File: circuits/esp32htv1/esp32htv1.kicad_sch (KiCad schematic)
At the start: 23 parts, among them J1 Power, SW1 SW_Push, U1 BME280, U2 ESP32-WROOM-32UE, U3 LD1117S33TR_SOT223

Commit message: Second version of the ESP32 HTV project
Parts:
- removed C11, C12, C13, C14, C15: 1 uF, Capacitor_SMD:C_1206_3216Metric_Pad1.33x1.80mm_HandSolder, symbol Device:C_Polarized
- removed U4: ~, gos:DOGM132-5, symbol gos:DOGM132
- added J2: UART, Connector_PinHeader_2.54mm:PinHeader_1x04_P2.54mm_Vertical, symbol Connector:Conn_01x04_Pin
- added P1: USB_C_Plug_USB2.0, symbol Connector:USB_C_Plug_USB2.0
- added SW2: BOOT, Connector_PinSocket_2.54mm:PinSocket_1x02_P2.54mm_Vertical, symbol Switch:SW_Push
- added U4: ~, gos:DOGS102-6, symbol gos:DOGS102
- J1, SW1: footprint Connector_PinHeader_1.00mm:PinHeader_1x02_P1.00mm_Vertical -> Connector_PinSocket_2.54mm:PinSocket_1x02_P2.54mm_Vertical
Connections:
- net +3V3: now also J2.1 (Pin_1), U4.22 (VDD), U4.23 (VDD2)
- net GND: now also J2.4 (Pin_4), SW2.2, U4.20 (VSS), U4.21 (VSS); no longer C8.2, C9.2
- net at C8.1: now also U4.17 (VB0-)
- net at C10.1: now also U4.15 (VLCD)
- net at C9.1: now also U4.16 (VB1-)
- net at U2.13 (IO14): now also U4.25 (SCK)
- net at U2.23 (IO15): now also U4.28 (CS0)
- net at U2.16 (IO13): now also U4.24 (SDA)
- net at U2.25 (IO0): now also SW2.1
- net at U2.27 (IO16): now also U4.26 (CD)
- net at U2.28 (IO17): now also U4.27 (RST)
- net at U2.34 (RXD0/IO3): now also J2.3 (Pin_3)
- net at U2.35 (TXD0/IO1): now also J2.2 (Pin_2)
- new net: C8.2, U4.18 (VB0+)
- new net: P1.A1 (GND), P1.A12 (GND), P1.B1 (GND), P1.B12 (GND)
- new net: P1.A4 (VBUS), P1.A9 (VBUS), P1.B4 (VBUS), P1.B9 (VBUS)
- new net: C9.2, U4.19 (VB1+)
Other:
- note removed: "LOW POWER CONFIGURATION"
- moved on the sheet: C10, C6, C7, C8, C9, U1

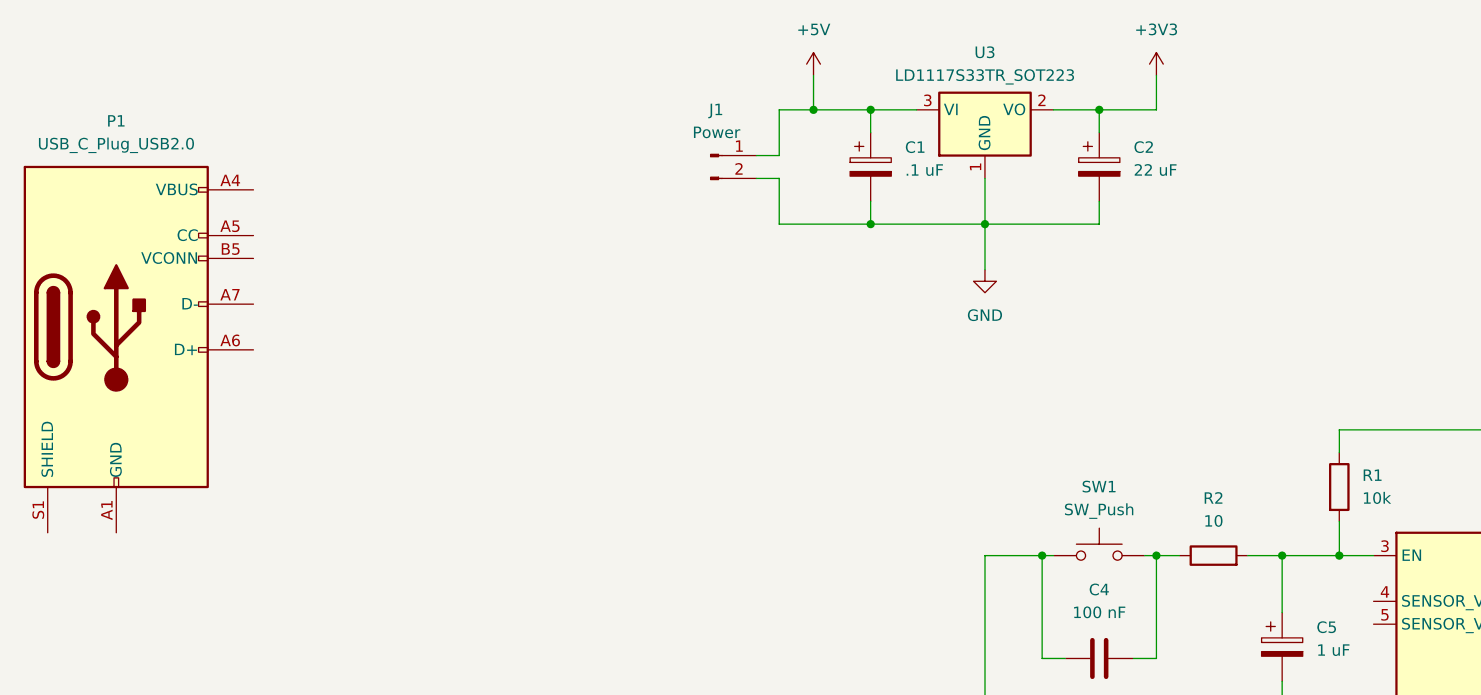
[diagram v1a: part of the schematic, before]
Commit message: Adding some sound effect circuits
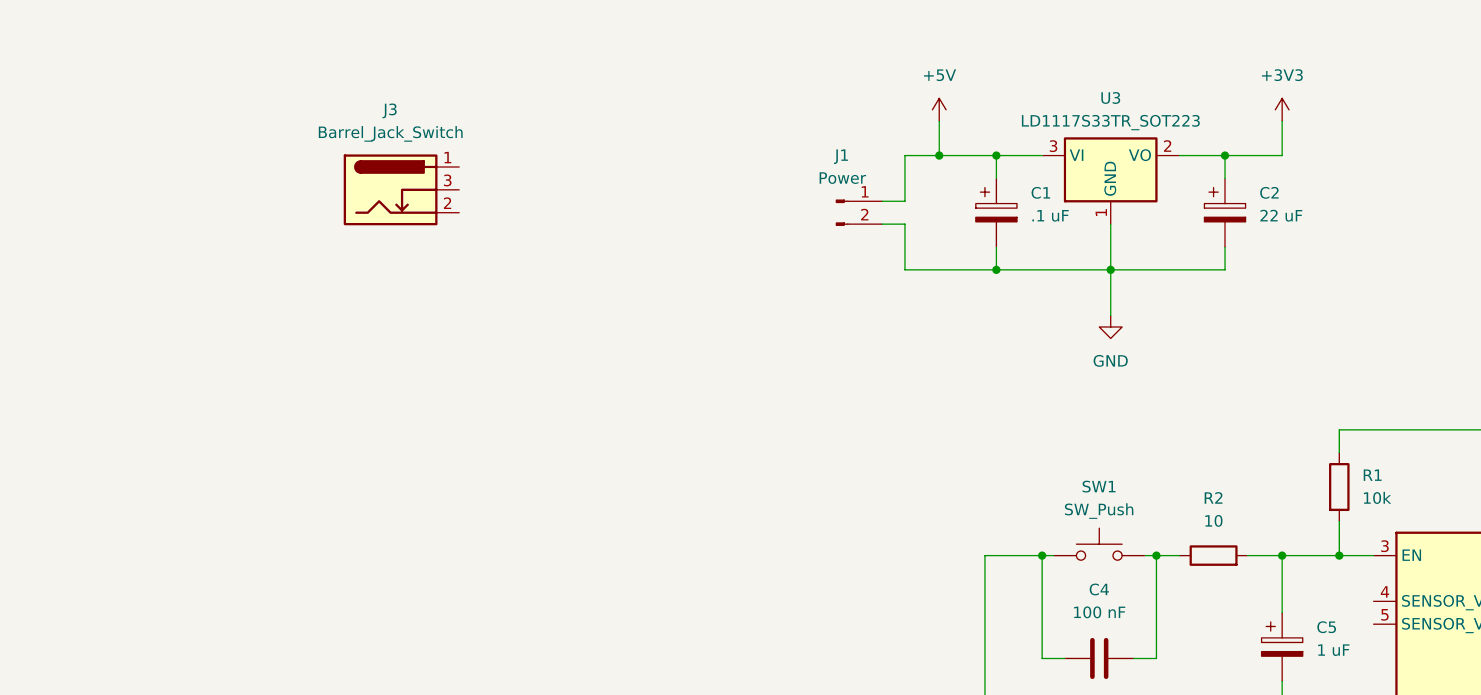
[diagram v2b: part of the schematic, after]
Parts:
- removed P1: USB_C_Plug_USB2.0, symbol Connector:USB_C_Plug_USB2.0
- added J3: Barrel_Jack_Switch, symbol Connector:Barrel_Jack_Switch
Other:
- moved on the sheet: C1, C2, J1, U3
